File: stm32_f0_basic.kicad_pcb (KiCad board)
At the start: 2 copper layers, 48 parts, among them J1 Conn_01x12_Male, J2 Conn_01x06_Male, J3 Conn_01x12_Male, J4 USB_B_Mini, J5 Conn_ARM_JTAG_SWD_10, SW1 B3S-1000P, SW2 B3S-1000P, U1 STM32F031K6Tx, U2 ADP121-AUJZ33R7, U3 FT230XS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

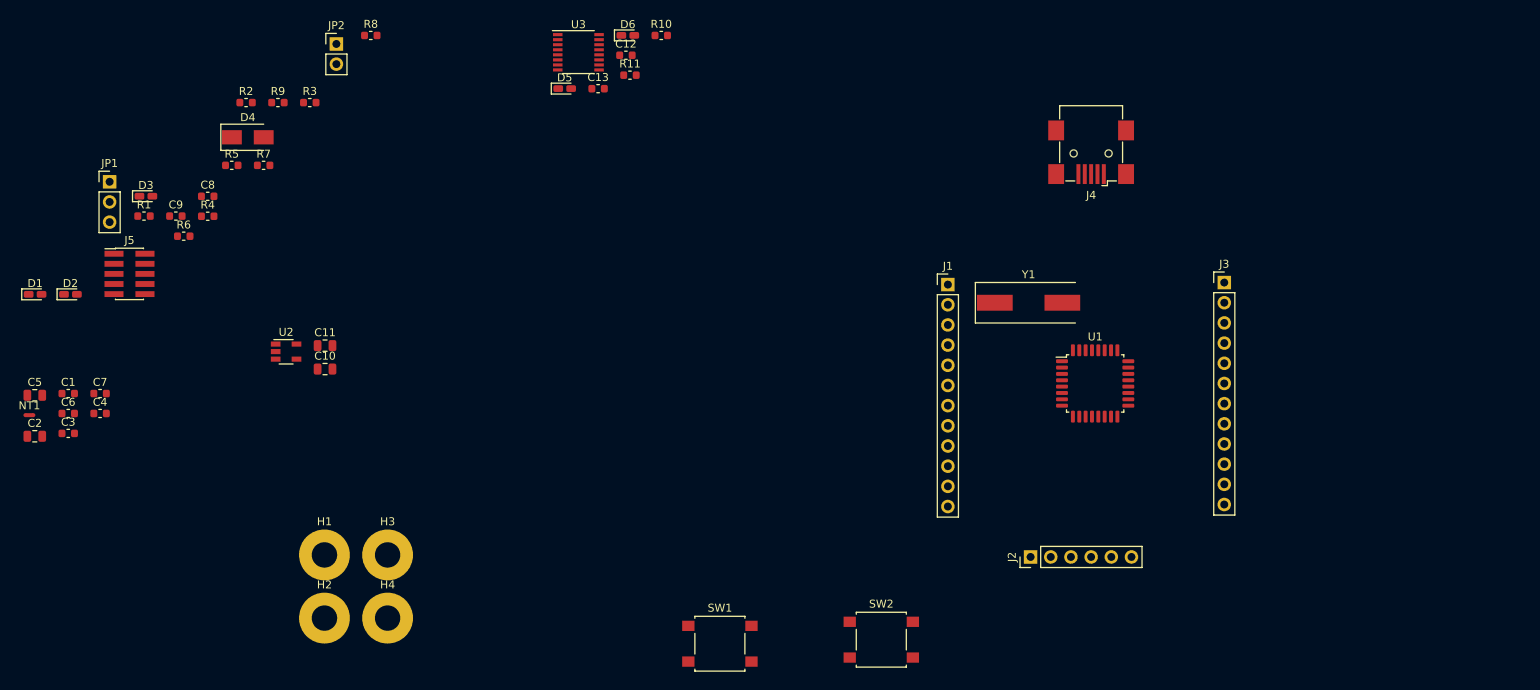
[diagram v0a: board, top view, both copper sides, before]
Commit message: complete initial layout
* components placed
* all nets routed
* switches, LEDs, connectors labeled
* TODO: route USB DM/DP as a diff pair?
* TODO: add 3D models for USB connector, pushbutton switches
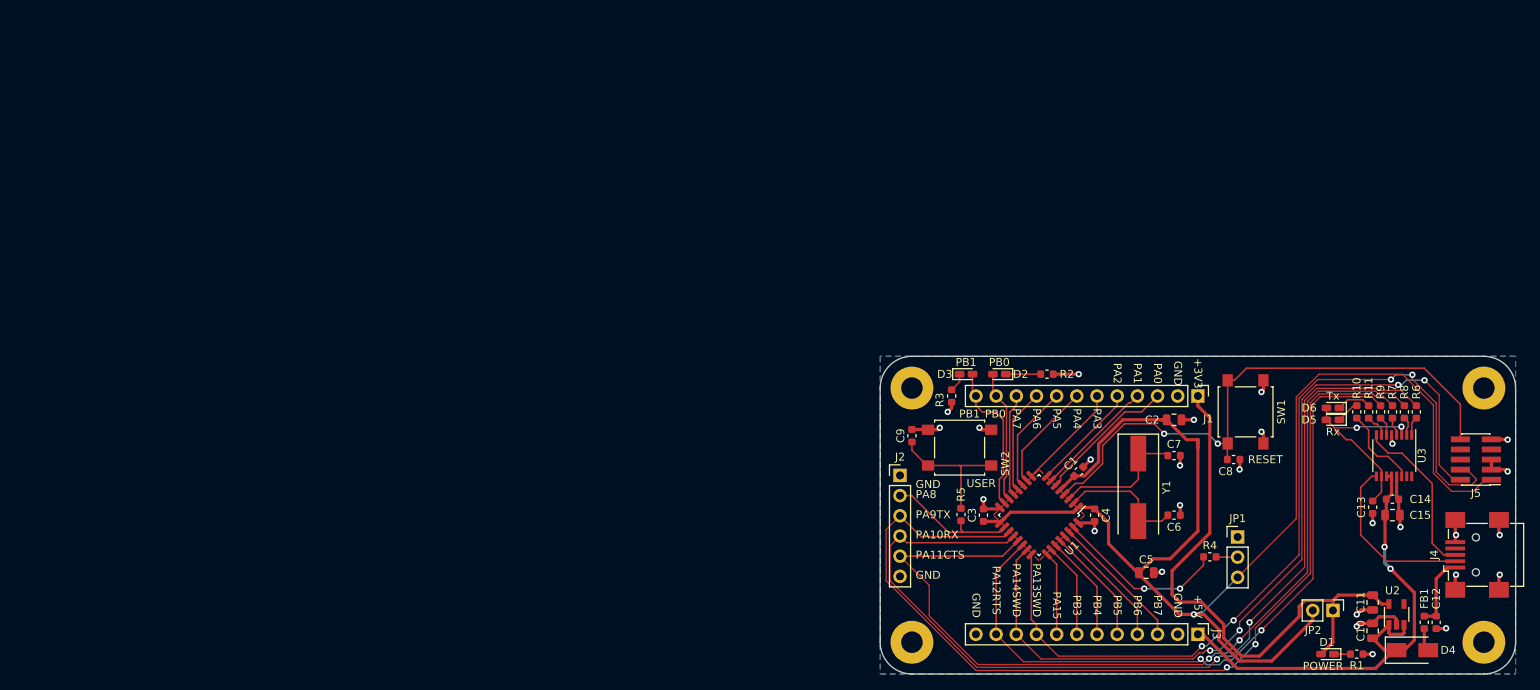
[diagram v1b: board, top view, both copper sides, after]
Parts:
- added C14: 100n, Capacitor_SMD:C_0603_1608Metric, F.Cu at (184.5, 73.0)
- added C15: 4.7u, Capacitor_SMD:C_0805_2012Metric, F.Cu at (184.5, 75.0)
- added FB1: Ferrite_Bead, Inductor_SMD:L_0603_1608Metric, F.Cu at (188.5, 88.5)
- H1, H2, H3, H4: footprint MountingHole:MountingHole_3.2mm_M3_Pad -> MountingHole:MountingHole_2.7mm_M2.5_Pad
- moved J5 171.1 mm to (195.0, 68.0), turned to 180 degrees
- moved D1 168.9 mm to (176.3, 92.5), turned to 180 degrees
- moved R1 162.3 mm to (180.0, 92.5), turned to 180 degrees
- moved D4 160.2 mm to (187.0, 92.0)
- moved R6 156.7 mm to (187.5, 62.0), turned to 90 degrees
- moved JP1 148.9 mm to (165.0, 77.8)
- moved H1 147.5 mm to (196.0, 59.0)
- moved NT1 147.2 mm to (160.0, 66.0), turned to 90 degrees
- moved H2 146.0 mm to (196.0, 91.0)
- moved R7 145.5 mm to (184.5, 62.0), turned to 90 degrees
- moved JP2 144.3 mm to (177.0, 87.0), turned to 270 degrees
- moved R9 144.2 mm to (183.0, 62.0), turned to 90 degrees
- moved U2 143.7 mm to (185.0, 87.5), turned to 90 degrees
- moved C2 143.4 mm to (157.0, 63.0)
- moved C5 141.7 mm to (153.5, 82.2)
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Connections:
- C12 pad 2: +5V -> Net-(C12-Pad2)
- J4 pad 1: Net-(D4-Pad2) -> Net-(C12-Pad2)
- R8 pad 2: GND -> /stm32f0/PA11_USART1_CTS
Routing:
- net VDD: track 0.00 -> 146.8 mm, vias 0 -> 1
- net /stm32f0/PA9_USART1_TX: track 0.00 -> 121.2 mm, vias 0 -> 2
- net /stm32f0/PA10_USART1_RX: track 0.00 -> 120.8 mm, vias 0 -> 2
- net /stm32f0/PA11_USART1_CTS: track 0.00 -> 114.6 mm, vias 0 -> 2
- net /stm32f0/PA14_SWDCLK: track 0.00 -> 107.1 mm, vias 0 -> 4
- net /stm32f0/PA13_SWDIO: track 0.00 -> 105.7 mm, vias 0 -> 4
- net /stm32f0/PA12_USART1_RTS: track 0.00 -> 90.2 mm, vias 0 -> 2
- net /stm32f0/NRST: track 0.00 -> 72.8 mm, vias 0 -> 2
- net +3V3: track 0.00 -> 70.9 mm
- net +5V: track 0.00 -> 64.2 mm, vias 0 -> 2
- net GND: track 0.00 -> 61.7 mm, vias 0 -> 27
- net Net-(C13-Pad2): track 0.00 -> 26.4 mm, vias 0 -> 2
- net VDDA: track 0.00 -> 23.3 mm
- net /stm32f0/BOOT0: track 0.00 -> 21.9 mm, vias 0 -> 2
- net /usb_uart/USB_DM: track 0.00 -> 21.8 mm
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- added copper zone on B.Cu, net GND
- added copper zone on F.Cu, net VDD
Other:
- board outline added: 80 x 40 mm
- net class Power added: clearance 0.2, trace_width 0.4064, via_dia 0.8, via_drill 0.4
- net class clk added: clearance 0.25, trace_width 0.2032, via_dia 0.8, via_drill 0.4
- net class gpio added: clearance 0.2, trace_width 0.2032, via_dia 0.8, via_drill 0.4
- net class usb added: clearance 0.2, trace_width 0.2032, via_dia 0.8, via_drill 0.4
- rule trace_min: 0.2 -> 0.1524
- board text added: "TODO USB diff pair? 3D models"

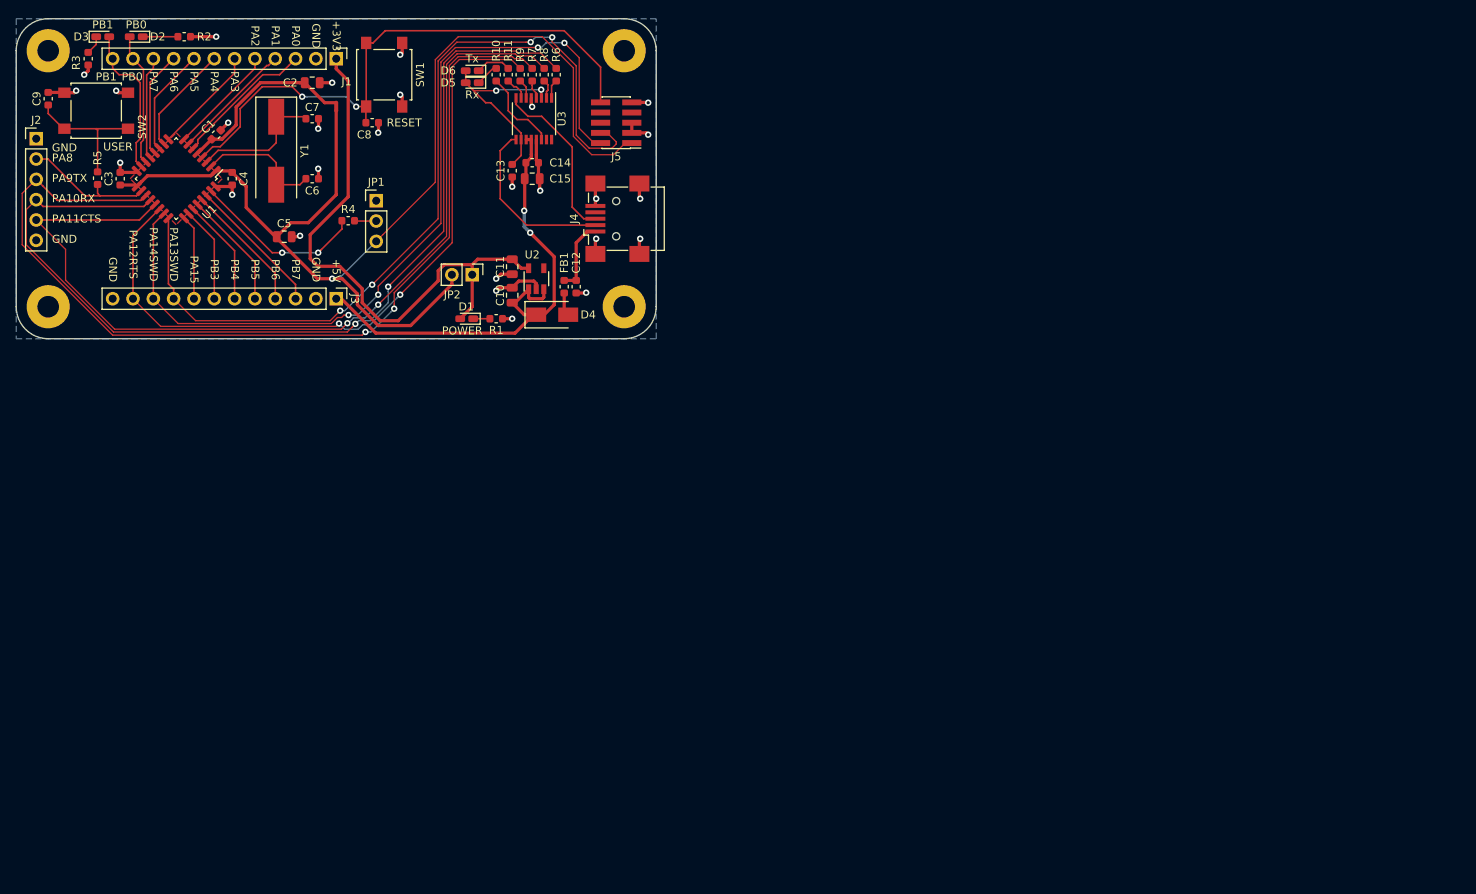
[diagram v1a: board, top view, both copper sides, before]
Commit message: rearrange headers and update silk labels (in progress)
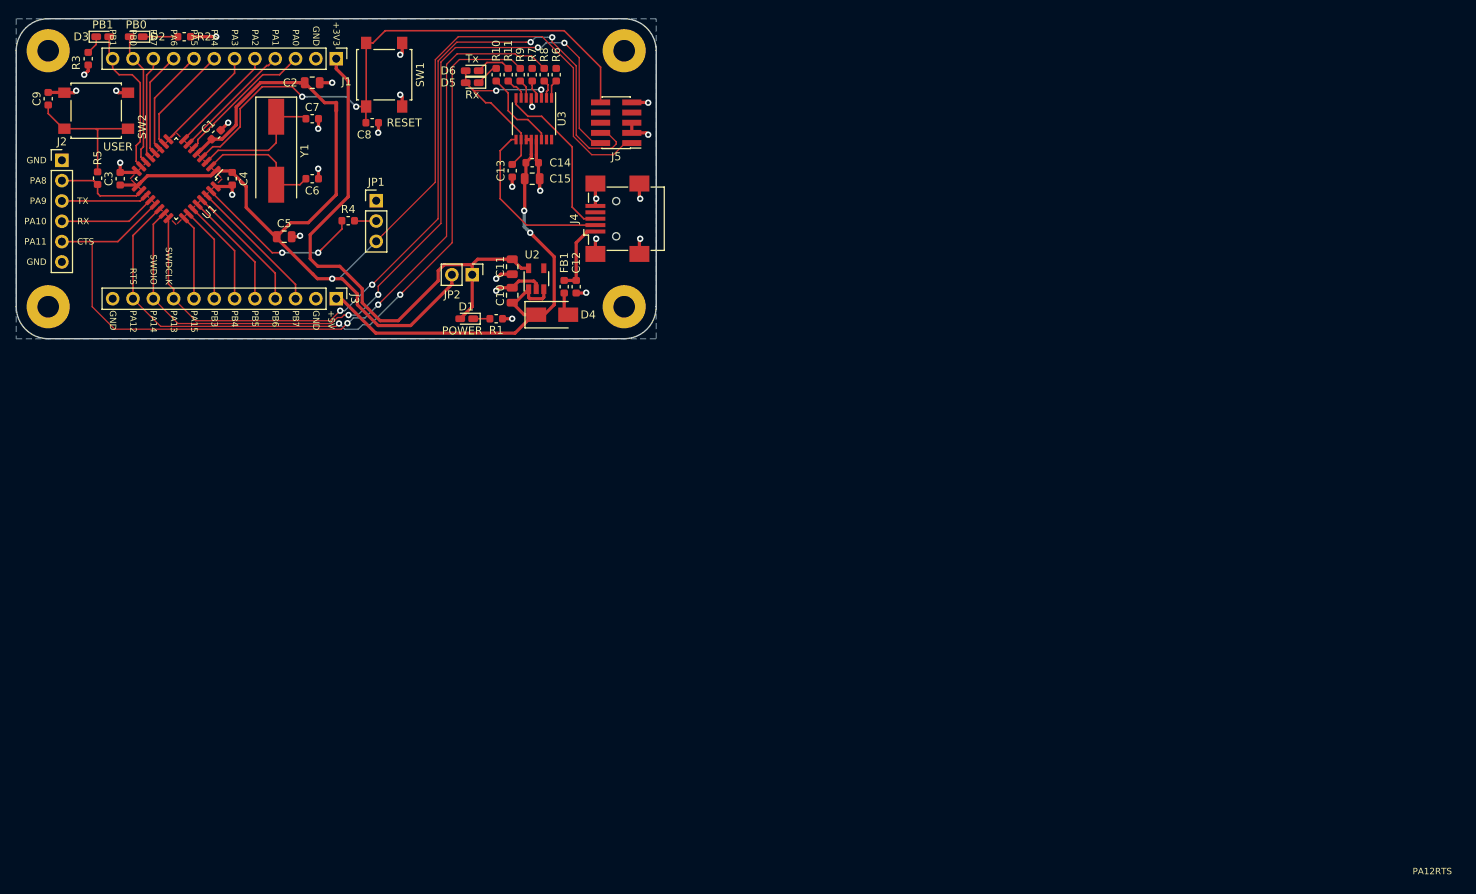
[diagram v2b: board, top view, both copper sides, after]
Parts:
- added ?: , , F.Cu at (130.8, 85.1)
- moved J2 4.19 mm to (125.7, 72.7)
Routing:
- net /stm32f0/PA9_USART1_TX: track 121.2 -> 10.8 mm, vias 2 -> 0
- net /stm32f0/PA10_USART1_RX: track 120.8 -> 12.2 mm, vias 2 -> 0
- net /stm32f0/PA11_USART1_CTS: track 114.6 -> 107.0 mm
- net /stm32f0/PA8: track 16.8 -> 11.6 mm

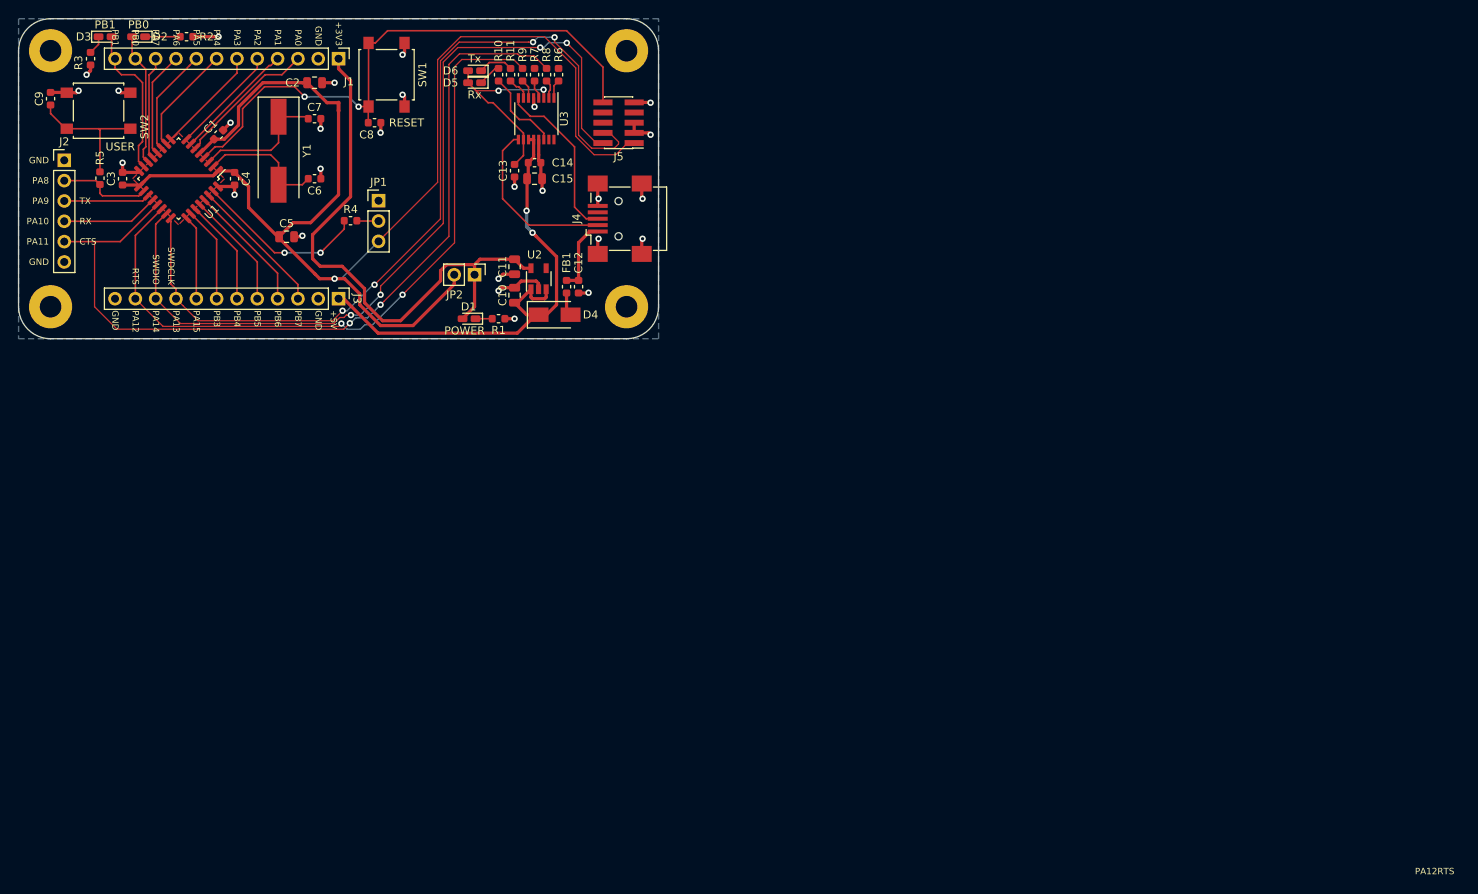
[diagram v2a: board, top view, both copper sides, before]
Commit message: Update USB schematic, redo lots of routing
* add series resistors and shunt capacitors to usb diff pair
* place usb-uart IC optimally for connecting to usb connector
* move bypass caps and resistors attached to usb-uart
* move user & reset buttons next to each other
* move user LEDs close to buttons
* move bottom connector
* redo associated routing
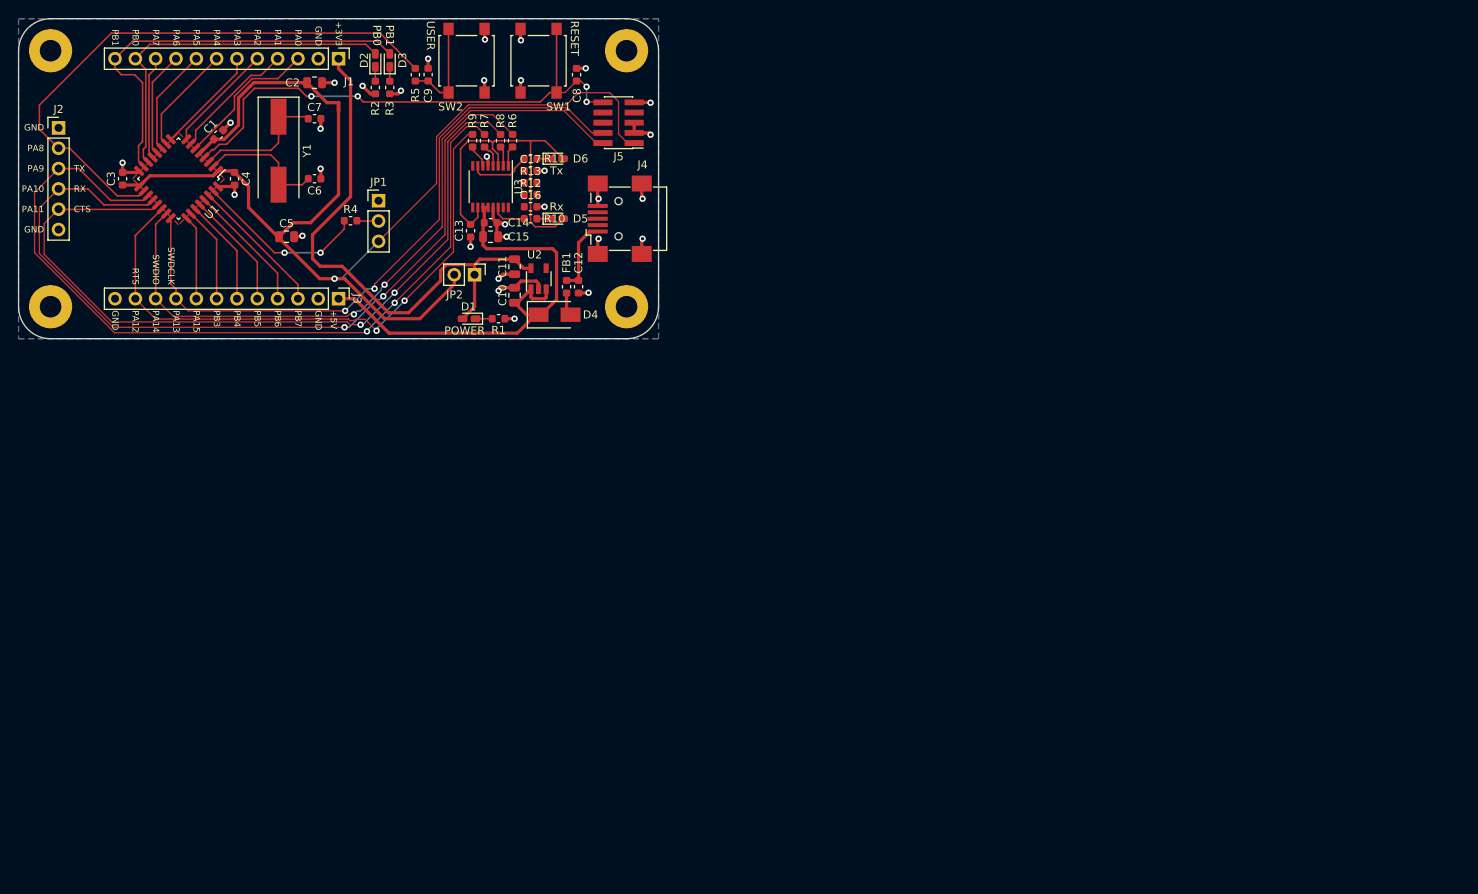
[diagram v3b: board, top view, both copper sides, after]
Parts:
- removed ?: , 
- added C16: 47pF, Capacitor_SMD:C_0603_1608Metric, F.Cu at (184.0, 78.5)
- added C17: 47pF, Capacitor_SMD:C_0603_1608Metric, F.Cu at (184.0, 74.0)
- added R12: 27, Resistor_SMD:R_0603_1608Metric, F.Cu at (184.0, 77.0)
- added R13: 27, Resistor_SMD:R_0603_1608Metric, F.Cu at (184.0, 75.5)
- moved C9 47.3 mm to (171.2, 62.0)
- moved SW2 46.4 mm to (176.0, 60.2), turned to 270 degrees
- moved R5 41.5 mm to (169.6, 62.0), turned to 90 degrees
- moved R3 37.6 mm to (166.4, 63.6)
- moved D3 35.7 mm to (166.4, 60.2), turned to 90 degrees
- moved D2 29.7 mm to (164.6, 60.2), turned to 90 degrees
- moved C8 26.0 mm to (189.8, 62.0), turned to 90 degrees
- moved R2 24.4 mm to (164.6, 63.6), turned to 90 degrees
- moved D5 19.9 mm to (187.2, 80.0), turned to 0 degrees
- moved SW1 19.1 mm to (185.0, 60.2), turned to 90 degrees
- moved R10 18.4 mm to (184.0, 80.0), turned to 0 degrees
- moved D6 15.0 mm to (187.2, 72.5), turned to 0 degrees
- moved R11 10.8 mm to (184.0, 72.5), turned to 0 degrees
- moved R7 10.4 mm to (178.2, 70.2)
- moved R9 10.4 mm to (176.8, 70.2)
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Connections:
- U3 pad 8: /usb_uart/USB_DP -> Net-(C17-Pad1)
- U3 pad 9: /usb_uart/USB_DM -> Net-(C16-Pad1)
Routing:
- net /stm32f0/PA9_USART1_TX: track 10.8 -> 104.0 mm, vias 0 -> 2
- net /stm32f0/PA10_USART1_RX: track 12.2 -> 103.8 mm, vias 0 -> 2
- net /stm32f0/PA8: track 11.6 -> 72.3 mm
- net /stm32f0/PB1: track 19.2 -> 52.2 mm
- net /stm32f0/PB0: track 16.7 -> 45.0 mm
- net /stm32f0/PA14_SWDCLK: track 107.1 -> 82.5 mm, vias 4 -> 2
- net /usb_uart/USB_DM: track 21.8 -> 0.00 mm
- net /usb_uart/USB_DP: track 21.1 -> 0.00 mm
- net /stm32f0/PA13_SWDIO: track 105.7 -> 86.9 mm, vias 4 -> 2
- net Net-(C13-Pad2): track 26.4 -> 44.9 mm, vias 2 -> 0
- net VDD: track 146.8 -> 130.1 mm
- net /stm32f0/PA12_USART1_RTS: track 90.2 -> 74.3 mm
- net /stm32f0/PA11_USART1_CTS: track 107.0 -> 97.9 mm
- net Net-(R10-Pad1): track 10.5 -> 4.31 mm
- net /stm32f0/NRST: track 72.8 -> 67.4 mm, vias 2 -> 4
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
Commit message: Route USB traces
* rename USB traces in schematic so they can be routed as a differential
pair
* route USB traces
* note: USB traces are routed as a differential pair, but not as a
transmission line of the correct 90R differential impedance, because
it's not feasible on a 2-layer, 1.6mm board (traces would be huge).
Doesn't matter for this short of a distance.
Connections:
- net /usb_uart/USB_DM renamed /usb_uart/USB_D-
- net /usb_uart/USB_DP renamed /usb_uart/USB_D+
- net Net-(C16-Pad1) renamed /usb_uart/USBUART-
- net Net-(C17-Pad1) renamed /usb_uart/USBUART+
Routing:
- net /usb_uart/USBUART+: track 0.00 -> 10.5 mm
- net /usb_uart/USBUART-: track 0.00 -> 9.98 mm
- net /usb_uart/USB_D-: track 0.00 -> 9.62 mm
- net /usb_uart/USB_D+: track 0.00 -> 9.62 mm
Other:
- board text added: "TODO 3D models"
- board text removed: "TODO USB diff pair? 3D models"
